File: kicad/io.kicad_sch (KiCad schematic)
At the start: 23 parts, among them J7 Conn_01x10_Pin, J9 Conn_01x10_Pin, U12 74LS573, U4 74LS573, U5 74HC245

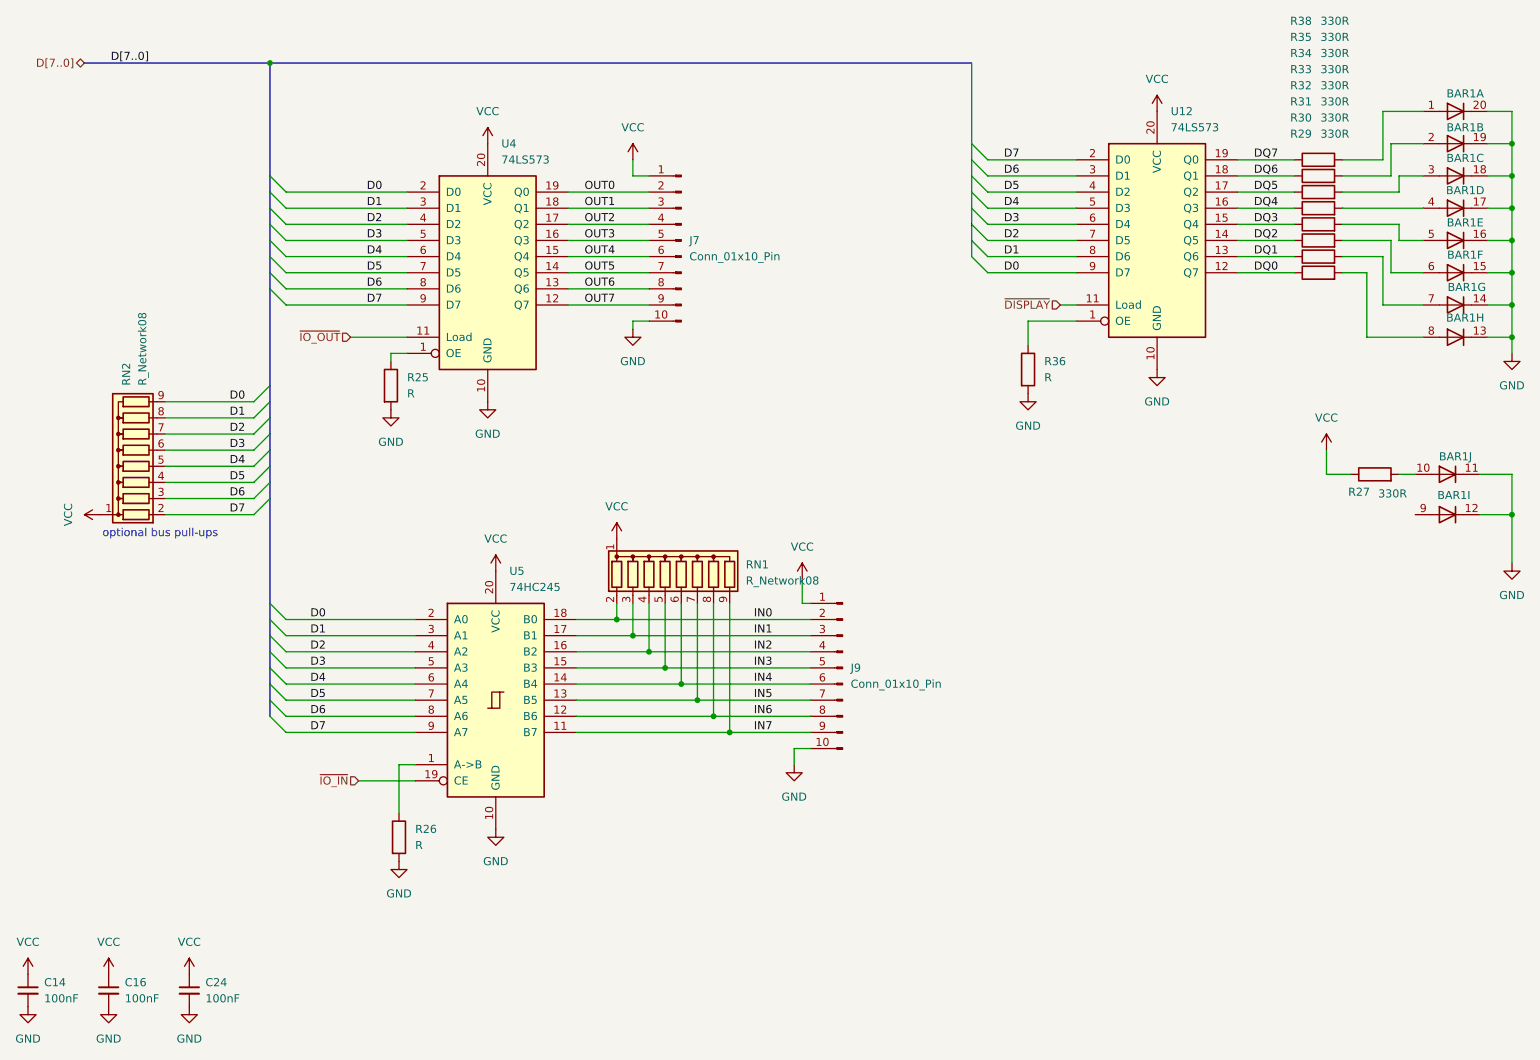
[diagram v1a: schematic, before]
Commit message: value updates, fix ROM ~WE
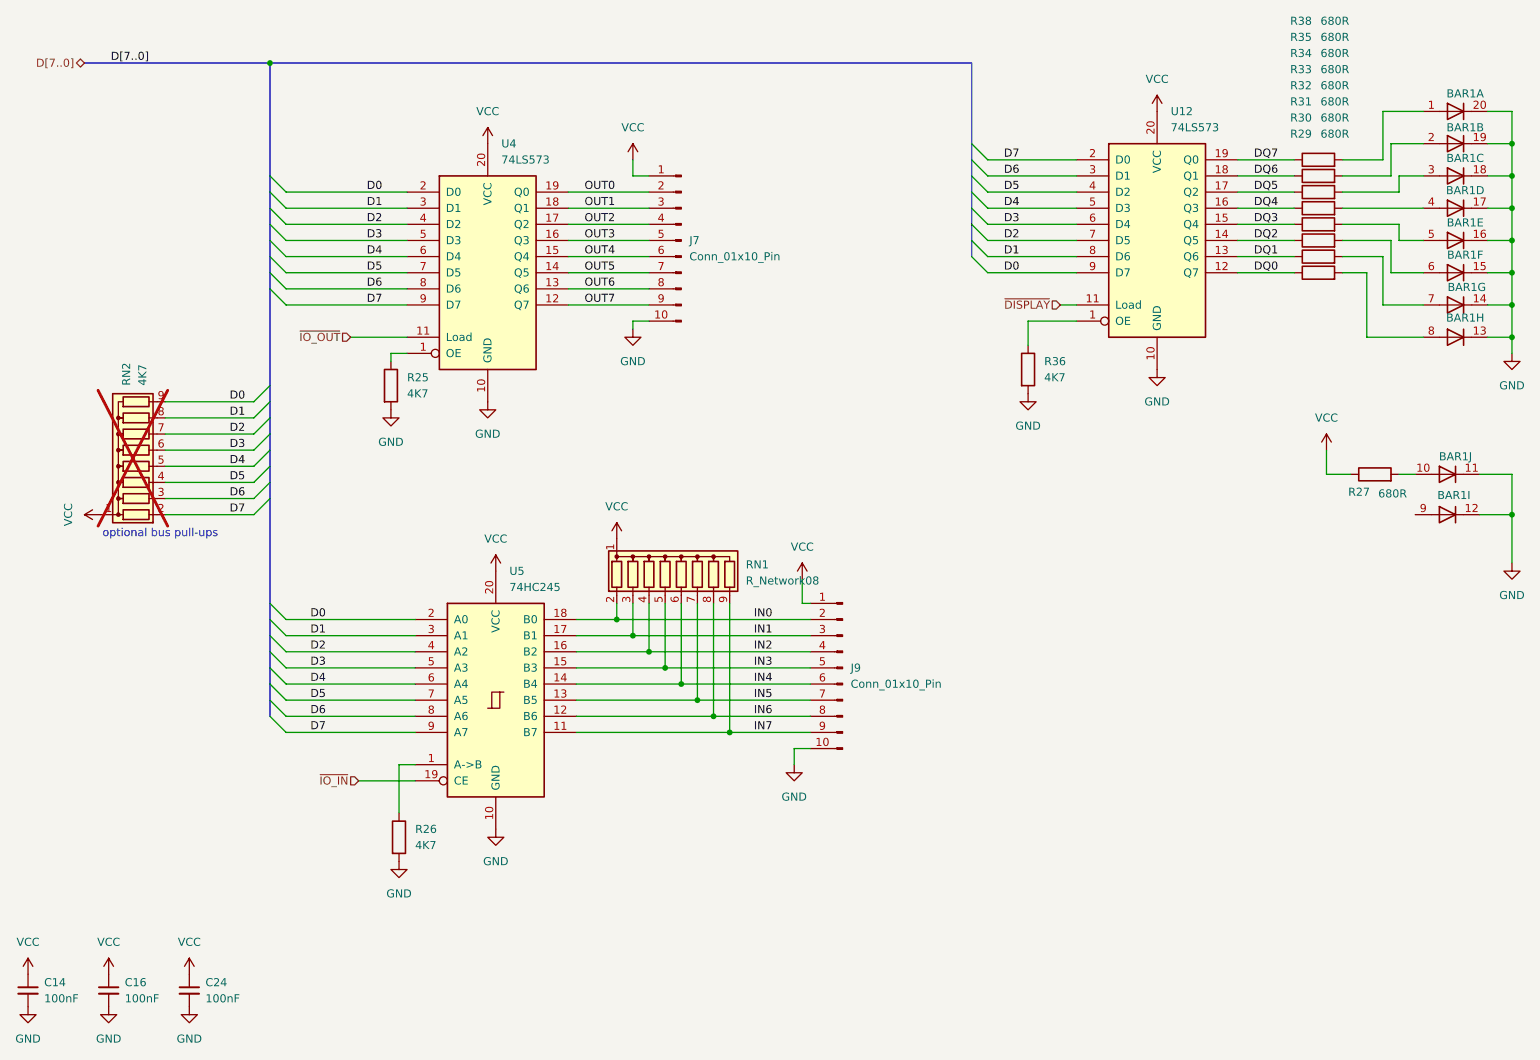
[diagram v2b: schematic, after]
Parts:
- R25, R26, R36: value R -> 4K7
- R27, R29, R30, R31, R32, R33, R34, R35, R38: value 330R -> 680R
- RN2: value R_Network08 -> 4K7; now not fitted
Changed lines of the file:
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@@
 			)
 		)
-		(property "Value" "330R"
+		(property "Value" "680R"
 			(at 241.554 99.568 90)
 			(effects
@@
 			)
 		)
-		(property "Value" "R"
+		(property "Value" "4K7"
 			(at 86.36 83.8199 0)
 			(effects
@@
 			)
 		)
-		(property "Value" "330R"
+		(property "Value" "680R"
 			(at 232.463 42.9183 90)
 			(effects
@@
 			)
 		)
-		(property "Value" "R"
+		(property "Value" "4K7"
 			(at 186.69 81.2799 0)
 			(effects
@@
 			)
 		)
-		(property "Value" "330R"
+		(property "Value" "680R"
 			(at 232.463 25.1383 90)
 			(effects
@@
 		(in_bom yes)
 		(on_board yes)
-		(dnp no)
+		(dnp yes)
 		(fields_autoplaced yes)
 		(property "Reference" "RN2"
@@
 			)
 		)
-		(property "Value" "R_Network08"
+		(property "Value" "4K7"
 			(at 44.7039 82.55 0)
 			(effects
@@
 			)
 		)
-		(property "Value" "330R"
+		(property "Value" "680R"
 			(at 232.463 37.8383 90)
 			(effects
@@
 			)
 		)
-		(property "Value" "R"
+		(property "Value" "4K7"
 			(at 87.63 154.9399 0)
 			(effects
@@
 			)
 		)
-		(property "Value" "330R"
+		(property "Value" "680R"
 			(at 232.463 27.6783 90)
 			(effects
@@
 			)
 		)
-		(property "Value" "330R"
+		(property "Value" "680R"
 			(at 232.463 35.2983 90)
 			(effects
@@
 			)
 		)
-		(property "Value" "330R"
+		(property "Value" "680R"
 			(at 232.463 30.2183 90)
 			(effects
@@
 			)
 		)
-		(property "Value" "330R"
+		(property "Value" "680R"
 			(at 232.463 32.7583 90)
 			(effects
@@
 			)
 		)
-		(property "Value" "330R"
+		(property "Value" "680R"
 			(at 232.463 40.3783 90)
 			(effects

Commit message: more updates for v1 rev2
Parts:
- removed R36: 4K7, Resistor_THT:R_Axial_DIN0207_L6.3mm_D2.5mm_P10.16mm_Horizontal, symbol Device:R
- R27, R29, R30, R31, R32, R33, R34, R35, R38: footprint Resistor_THT:R_Axial_DIN0207_L6.3mm_D2.5mm_P10.16mm_Horizontal -> Resistor_THT:R_Axial_DIN0207_L6.3mm_D2.5mm_P2.54mm_Vertical
- U12, U4: value 74LS573 -> 74LS574
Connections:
- net GND: now also U12.1 (OE)
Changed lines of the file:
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@@
 	(wire
 		(pts
-			(xy 184.15 72.39) (xy 184.15 76.2)
+			(xy 189.23 72.39) (xy 189.23 76.2)
 		)
 		(stroke
@@
 	(wire
 		(pts
-			(xy 191.77 72.39) (xy 184.15 72.39)
+			(xy 191.77 72.39) (xy 189.23 72.39)
 		)
 		(stroke
@@
 	(symbol
 		(lib_id "power:GND")
-		(at 184.15 83.82 0)
+		(at 189.23 76.2 0)
 		(unit 1)
 		(exclude_from_sim no)
@@
 		(fields_autoplaced yes)
 		(property "Reference" "#PWR050"
-			(at 184.15 90.17 0)
+			(at 189.23 82.55 0)
 			(effects
 				(font
@@
 		)
 		(property "Value" "GND"
-			(at 184.15 88.9 0)
+			(at 189.23 81.28 0)
 			(effects
 				(font
@@
 		)
 		(property "Footprint" ""
-			(at 184.15 83.82 0)
+			(at 189.23 76.2 0)
 			(effects
 				(font
@@
 		)
 		(property "Datasheet" ""
-			(at 184.15 83.82 0)
+			(at 189.23 76.2 0)
 			(effects
 				(font
@@
 		)
 		(property "Description" "Power symbol creates a global label with name \"GND\" , ground"
-			(at 184.15 83.82 0)
+			(at 189.23 76.2 0)
 			(effects
 				(font
@@
 			)
 		)
-		(property "Footprint" "Resistor_THT:R_Axial_DIN0207_L6.3mm_D2.5mm_P10.16mm_Horizontal"
+		(property "Footprint" "Resistor_THT:R_Axial_DIN0207_L6.3mm_D2.5mm_P2.54mm_Vertical"
 			(at 238.76 98.298 90)
 			(effects
@@
 			)
 		)
-		(property "Value" "74LS573"
+		(property "Value" "74LS574"
 			(at 101.2033 46.99 0)
 			(effects
@@
 			)
 		)
-		(property "Value" "74LS573"
+		(property "Value" "74LS574"
 			(at 206.6133 41.91 0)
 			(effects
@@
 			)
 		)
-		(property "Footprint" "Resistor_THT:R_Axial_DIN0207_L6.3mm_D2.5mm_P10.16mm_Horizontal"
+		(property "Footprint" "Resistor_THT:R_Axial_DIN0207_L6.3mm_D2.5mm_P2.54mm_Vertical"
 			(at 229.87 66.548 90)
 			(effects
@@
 	)
 	(symbol
-		(lib_id "Device:R")
-		(at 184.15 80.01 0)
-		(unit 1)
-		(exclude_from_sim no)
-		(in_bom yes)
-		(on_board yes)
-		(dnp no)
-		(fields_autoplaced yes)
-		(property "Reference" "R36"
-			(at 186.69 78.7399 0)
-			(effects
-				(font
-					(size 1.27 1.27)
-				)
-				(justify left)
-			)
-		)
-		(property "Value" "4K7"
-			(at 186.69 81.2799 0)
-			(effects
-				(font
-					(size 1.27 1.27)
-				)
-				(justify left)
-			)
-		)
-		(property "Footprint" "Resistor_THT:R_Axial_DIN0207_L6.3mm_D2.5mm_P10.16mm_Horizontal"
-			(at 182.372 80.01 90)
-			(effects
-				(font
-					(size 1.27 1.27)
-				)
-				(hide yes)
-			)
-		)
-		(property "Datasheet" "~"
-			(at 184.15 80.01 0)
-			(effects
-				(font
-					(size 1.27 1.27)
-				)
-				(hide yes)
-			)
-		)
-		(property "Description" "Resistor"
-			(at 184.15 80.01 0)
-			(effects
-				(font
-					(size 1.27 1.27)
-				)
-				(hide yes)
-			)
-		)
-		(pin "2"
-		)
-		(pin "1"
-		)
-		(instances
-			(project "6502atty"
-				(path "/f612fa92-d5fa-4cb5-a666-c1c24e7cbb30/77244e5e-10b6-41b8-8f57-dd636697e539"
-					(reference "R36")
-					(unit 1)
-				)
-			)
-		)
-	)
-	(symbol
 		(lib_id "power:VCC")
 		(at 148.59 113.03 0)
@@
 			)
 		)
-		(property "Footprint" "Resistor_THT:R_Axial_DIN0207_L6.3mm_D2.5mm_P10.16mm_Horizontal"
+		(property "Footprint" "Resistor_THT:R_Axial_DIN0207_L6.3mm_D2.5mm_P2.54mm_Vertical"
 			(at 229.87 48.768 90)
 			(effects
@@
 			)
 		)
-		(property "Footprint" "Resistor_THT:R_Axial_DIN0207_L6.3mm_D2.5mm_P10.16mm_Horizontal"
+		(property "Footprint" "Resistor_THT:R_Axial_DIN0207_L6.3mm_D2.5mm_P2.54mm_Vertical"
 			(at 229.87 61.468 90)
 			(effects
@@
 			)
 		)
-		(property "Footprint" "Resistor_THT:R_Axial_DIN0207_L6.3mm_D2.5mm_P10.16mm_Horizontal"
+		(property "Footprint" "Resistor_THT:R_Axial_DIN0207_L6.3mm_D2.5mm_P2.54mm_Vertical"
 			(at 229.87 51.308 90)
 			(effects
@@
 			)
 		)
-		(property "Footprint" "Resistor_THT:R_Axial_DIN0207_L6.3mm_D2.5mm_P10.16mm_Horizontal"
+		(property "Footprint" "Resistor_THT:R_Axial_DIN0207_L6.3mm_D2.5mm_P2.54mm_Vertical"
 			(at 229.87 58.928 90)
 			(effects
@@
 			)
 		)
-		(property "Footprint" "Resistor_THT:R_Axial_DIN0207_L6.3mm_D2.5mm_P10.16mm_Horizontal"
+		(property "Footprint" "Resistor_THT:R_Axial_DIN0207_L6.3mm_D2.5mm_P2.54mm_Vertical"
 			(at 229.87 53.848 90)
 			(effects
@@
 			)
 		)
-		(property "Footprint" "Resistor_THT:R_Axial_DIN0207_L6.3mm_D2.5mm_P10.16mm_Horizontal"
+		(property "Footprint" "Resistor_THT:R_Axial_DIN0207_L6.3mm_D2.5mm_P2.54mm_Vertical"
 			(at 229.87 56.388 90)
 			(effects
@@
 			)
 		)
-		(property "Footprint" "Resistor_THT:R_Axial_DIN0207_L6.3mm_D2.5mm_P10.16mm_Horizontal"
+		(property "Footprint" "Resistor_THT:R_Axial_DIN0207_L6.3mm_D2.5mm_P2.54mm_Vertical"
 			(at 229.87 64.008 90)
 			(effects
